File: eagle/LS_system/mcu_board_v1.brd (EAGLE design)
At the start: 47 x 31.8 mm, 24 parts, among them IC2 LT1763CS8-3.3, IC3 STM32F4XX_64, Q2 PFET, X1 USBSMD, X2 MURDOCK_STACK

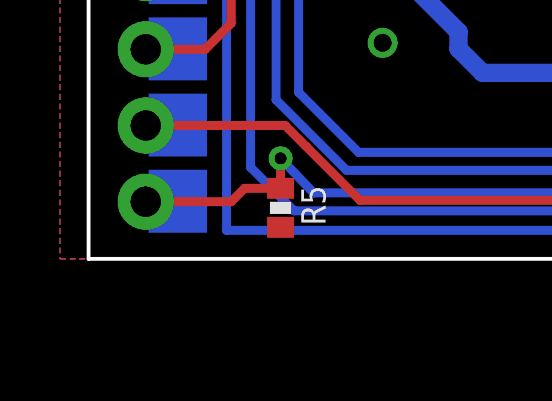
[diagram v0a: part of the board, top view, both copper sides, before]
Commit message: conneced LEDs to switche 3v3
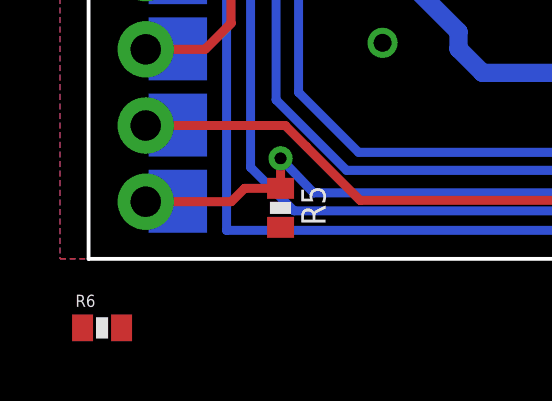
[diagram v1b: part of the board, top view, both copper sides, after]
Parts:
- added R6: 15k, SparkFun-Resistors:0402-RES
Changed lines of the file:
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@@
 <?xml version="1.0" encoding="utf-8"?>
 <!DOCTYPE eagle SYSTEM "eagle.dtd">
-<eagle version="6.4">
+<eagle version="6.3">
 <drawing>
 <settings>
@@
 <attribute name="VALUE" x="7.543" y="0.6205" size="0.4064" layer="27" rot="R90"/>
 </element>
+<element name="R6" library="SparkFun-Resistors" package="0402-RES" value="15k" x="0.45" y="-2.3"/>
 </elements>
 <signals>

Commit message: typo
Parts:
- removed R6: 15k, SparkFun-Resistors:0402-RES
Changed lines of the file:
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@@
 <attribute name="VALUE" x="7.543" y="0.6205" size="0.4064" layer="27" rot="R90"/>
 </element>
-<element name="R6" library="SparkFun-Resistors" package="0402-RES" value="15k" x="0.45" y="-2.3"/>
 </elements>
 <signals>
